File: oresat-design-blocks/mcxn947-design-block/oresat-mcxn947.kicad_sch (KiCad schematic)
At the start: 67 parts, among them J1 BKUP-BATT, J2 USB_C_Receptacle_USB2.0_14P, J3 CAN, J4 TERM, J5 10pin ARM SWD, J6 FTDI-UART-6PIN, SW1 RESET, SW2 ISP(BOOT), U1 MCXN947VKLT, U2 TCAN330, Y1 24 MHz, Y2 32.768 KHz

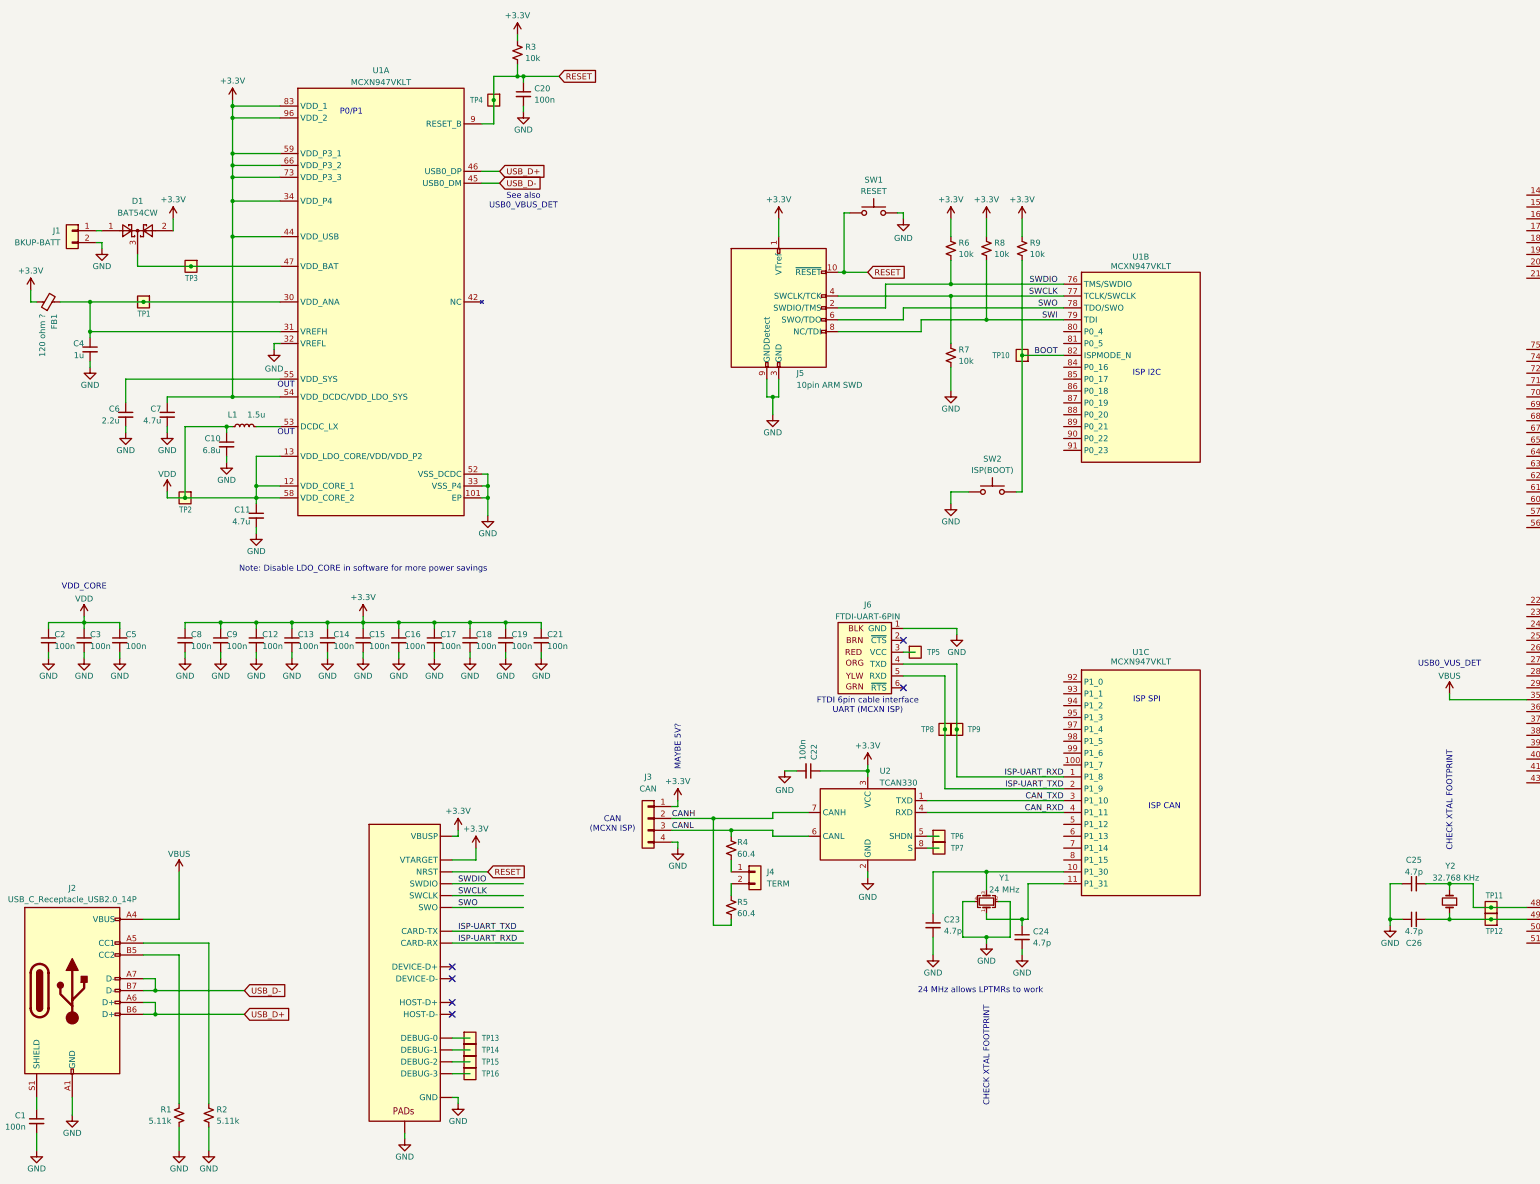
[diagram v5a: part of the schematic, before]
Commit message: Added 3.3V SPS but not hooked up yet. Everything else a rough draft, except for pin breakouts.
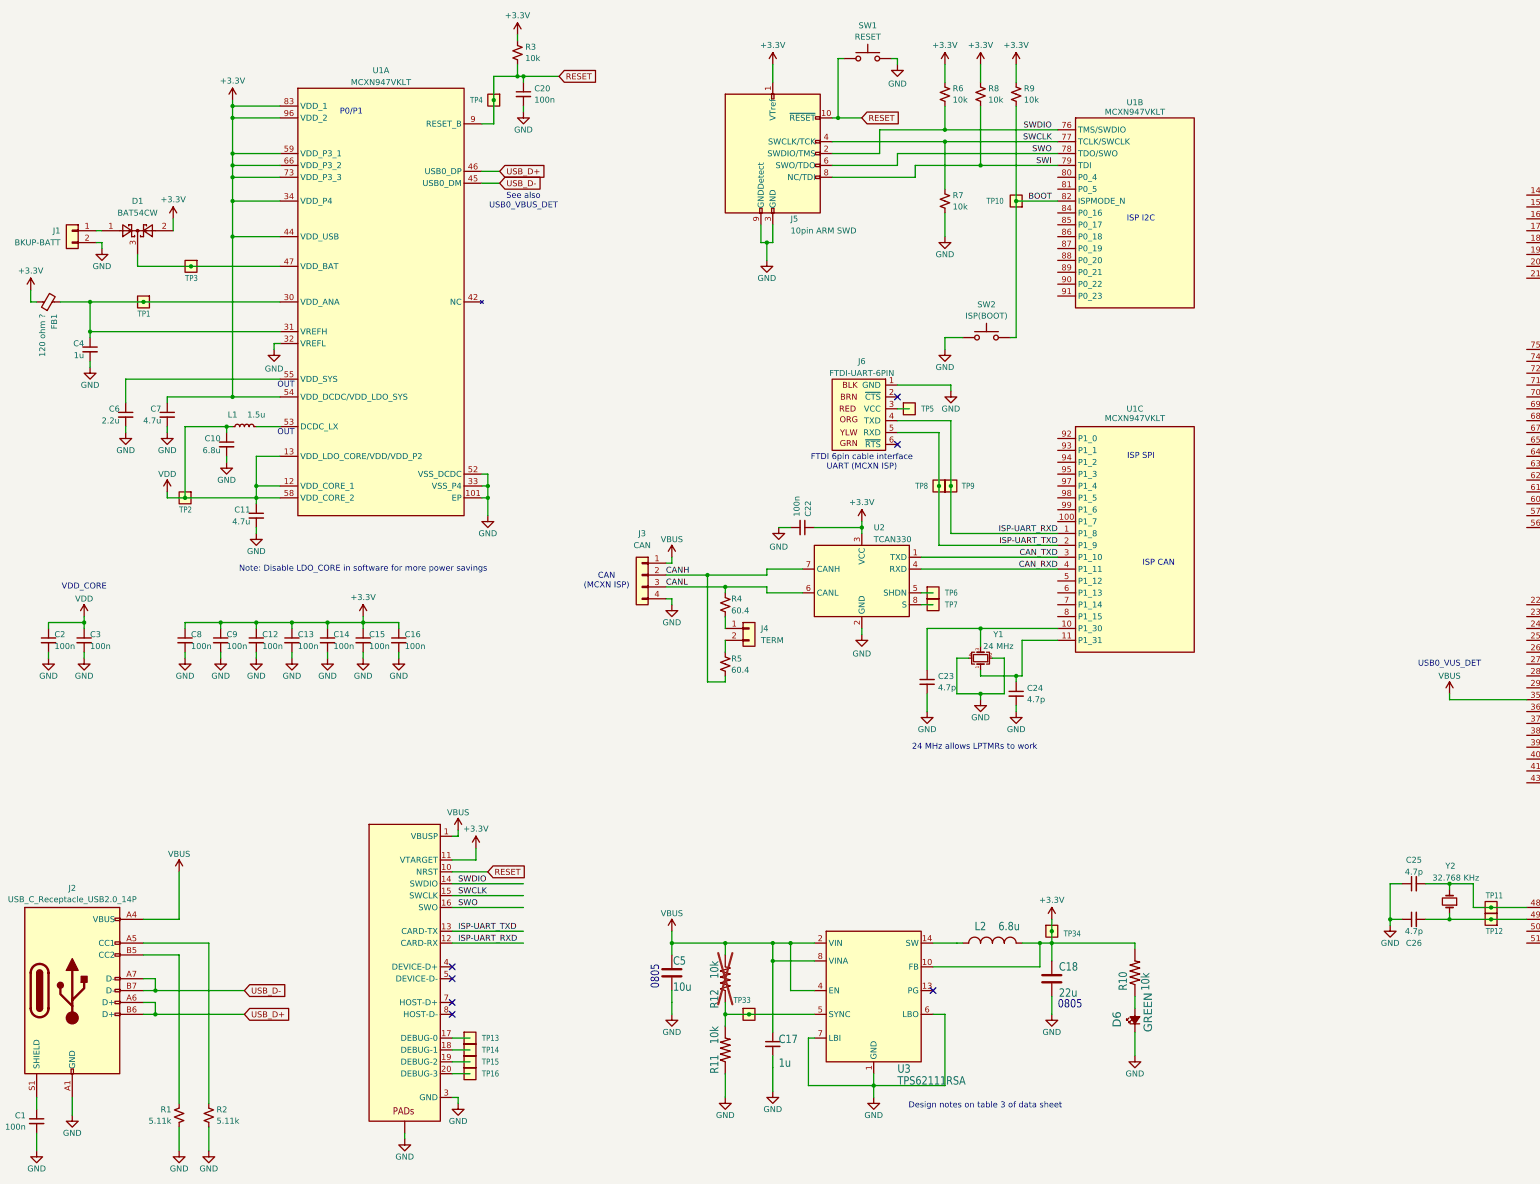
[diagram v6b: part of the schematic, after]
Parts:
- removed C18, C19, C21, C5: 100n, oresat-passives:0603-B-NOSILK, symbol Device:C_Small
- added C18: 22u, oresat-passives:0805-B-NOSILK, symbol Device:C
- added C5: 10u, oresat-passives:0805-B-NOSILK, symbol Device:C
- added D6: GREEN, LED_SMD:LED_0603_1608Metric, symbol Device:LED_Small_Filled
- added L2: 6.8u, oresat-passives:L_ECS-MPI4040, symbol oresat-passives:L_BIG
- added R10, R11, R12: 10k, oresat-passives:0603-C-NOSILK, symbol oresat-passives:R-US
- added TP33, TP34: Test-Point, oresat-misc:TestPoint-0.75mm-th, symbol oresat-misc:Test-Point-0.75mm-th
- added U3: TPS62111RSA, Package_DFN_QFN:Texas_RSA_VQFN-16-1EP_4x4mm_P0.65mm_EP2.7x2.7mm, symbol oresat-ics:TPS6211X
- C17: value 100n -> 1u; footprint oresat-passives:0603-B-NOSILK -> oresat-passives:0603-C-NOSILK; DIS (none) -> Digi-Key; DPN (none) -> 311-1444-1-ND; MFR (none) -> Yageo; MPN (none) -> CC0603KRX5R7BB105
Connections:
- net +3.3V: now also C18.1, L2.2, R10.2, TP34.1, U3.10 (FB); no longer C17.1, J3.1 (Pin_1), J7.1 (VBUSP), J7.2 (VBUSP)
- net GND: now also C18.2, C5.2, D6.1 (K), R11.1, U3.1 (GND), U3.11 (GND), U3.12 (GND), U3.16 (GND), U3.17 (GND), U3.6 (LBO), U3.7 (LBI), U3.9 (GND)
- net VBUS: now also C17.1, J3.1 (Pin_1), J7.1 (VBUSP), J7.2 (VBUSP), C5.1, R12.2, U3.2 (VIN), U3.3 (VIN), U3.4 (EN), U3.8 (VINA)
- new net: L2.1, U3.14 (SW), U3.15 (SW)
- new net: R11.2, R12.1, TP33.1, U3.5 (SYNC)
- new net: D6.2 (A), R10.1
- no-connect marks 6 -> 7
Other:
- note added: "0805"
- note added: "Design notes on table 3 of data sheet"
- note removed: "CHECK XTAL FOOTPRINT"
- note removed: "MAYBE 5V?"
- moved on the sheet: C22, C23, C24, J3, J4, J5, J6, R4, R5, R6, R7, R8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

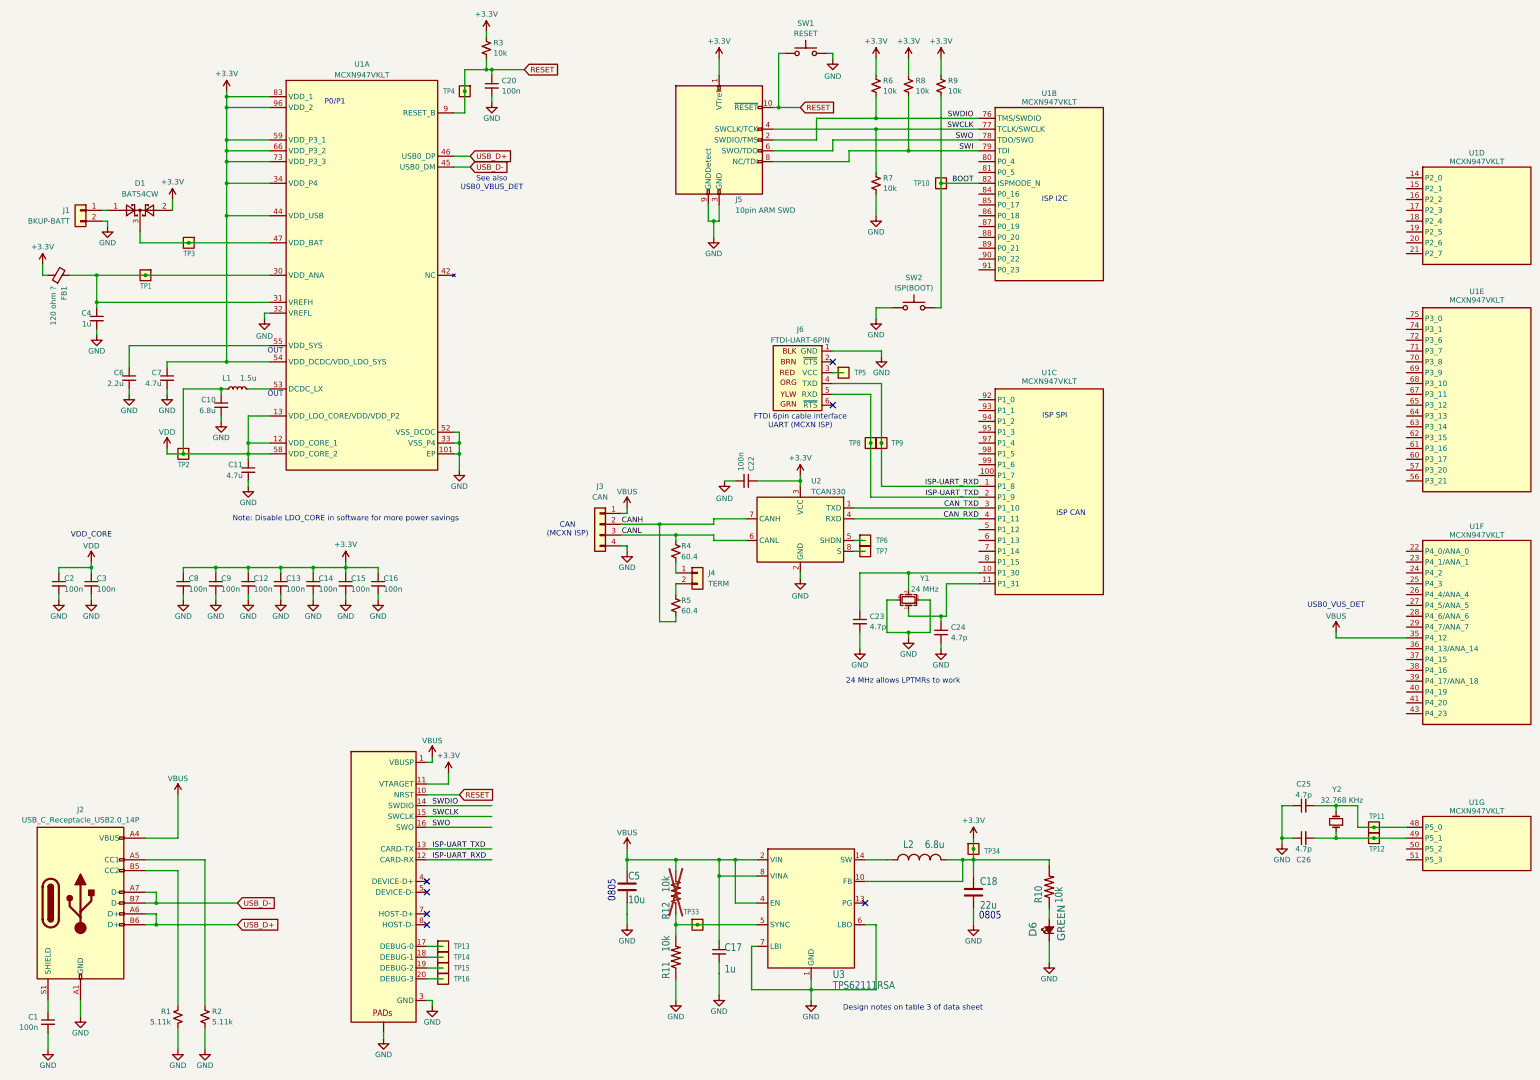
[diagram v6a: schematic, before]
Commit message: added hierarchal sheets, cleaned up schematic, added and routed breakout connectors
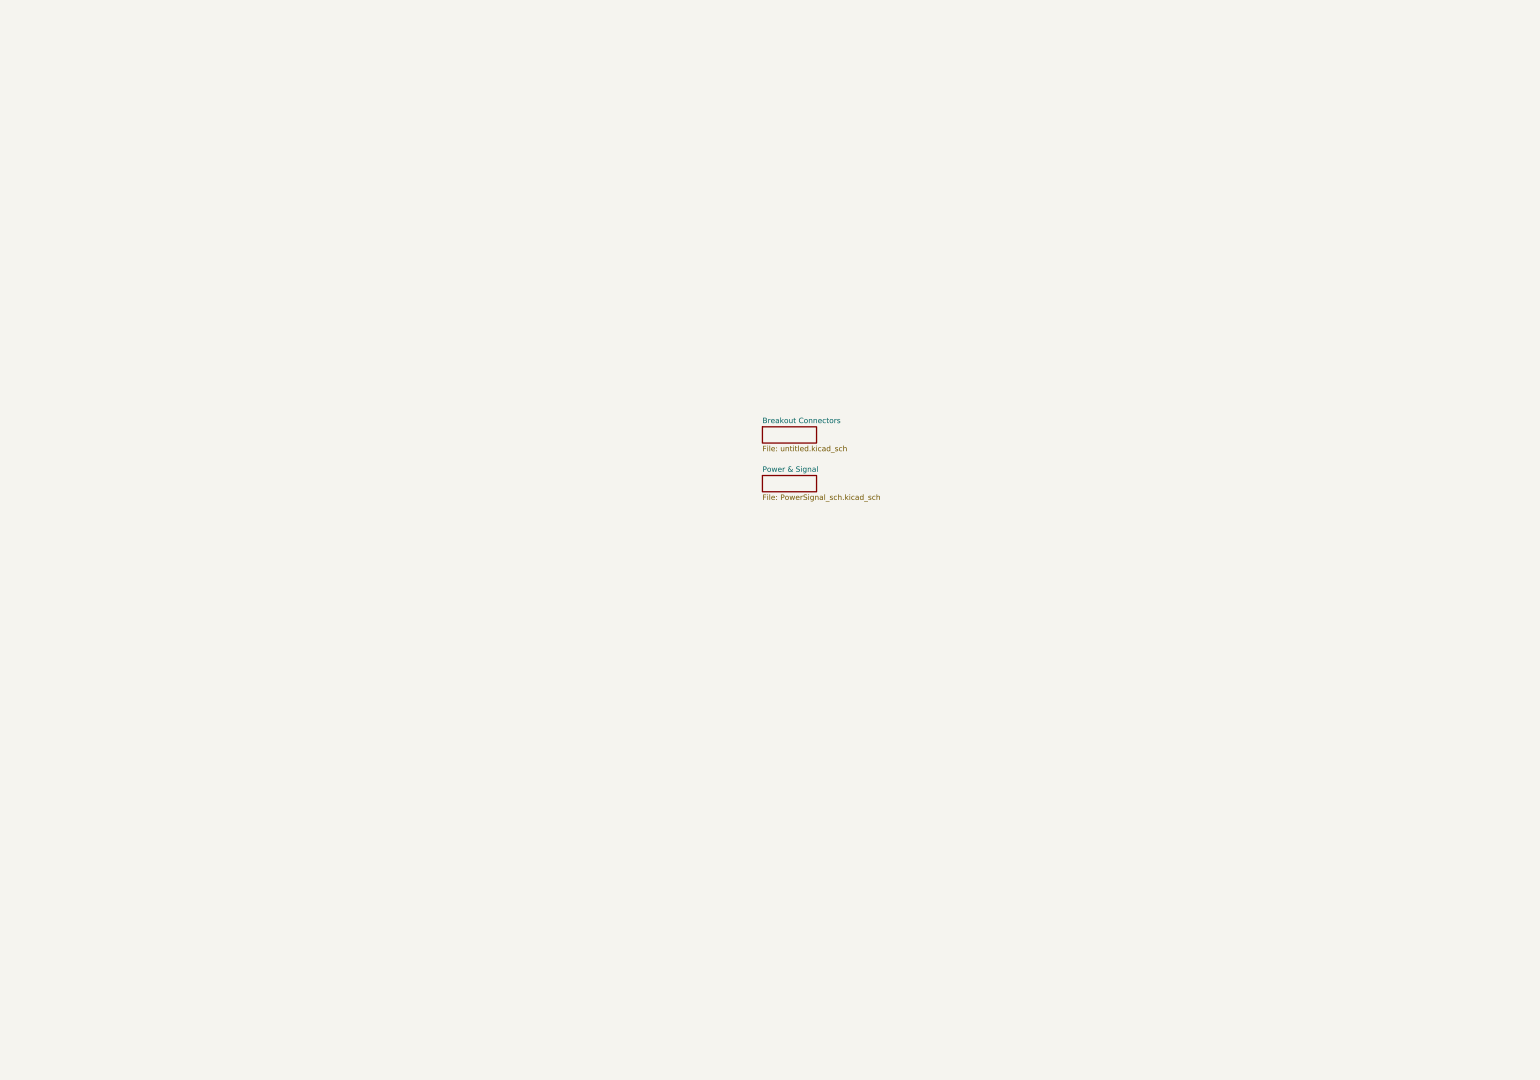
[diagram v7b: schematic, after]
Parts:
- removed C1, C12, C13, C14, C15, C16, C2, C20, C22, C3, C8, C9: 100n, oresat-passives:0603-B-NOSILK, symbol Device:C_Small
- removed C10: 6.8u, oresat-passives:0603-B-NOSILK, symbol Device:C_Small
- removed C11, C7: 4.7u, oresat-passives:0603-B-NOSILK, symbol Device:C_Small
- removed C17: 1u, oresat-passives:0603-C-NOSILK, symbol Device:C_Small
- removed C18: 22u, oresat-passives:0805-B-NOSILK, symbol Device:C
- removed C23, C24, C25, C26: 4.7p, oresat-passives:0603-B-NOSILK, symbol Device:C_Small
- removed C4: 1u, oresat-passives:0603-B-NOSILK, symbol Device:C_Small
- removed C5: 10u, oresat-passives:0805-B-NOSILK, symbol Device:C
- removed C6: 2.2u, oresat-passives:0603-B-NOSILK, symbol Device:C_Small
- removed D1: BAT54CW, oresat-passives:PAT0816(0603), symbol Diode:BAT54CW
- removed D6: GREEN, LED_SMD:LED_0603_1608Metric, symbol Device:LED_Small_Filled
- removed FB1: 120 ohm ?, oresat-passives:0805-B-NOSILK, symbol Device:FerriteBead_Small
- removed J1: BKUP-BATT, Connector_PinHeader_2.54mm:PinHeader_1x02_P2.54mm_Vertical, symbol Connector_Generic:Conn_01x02
- removed J2: USB_C_Receptacle_USB2.0_14P, Connector_USB:USB_C_Receptacle_Palconn_UTC16-G, symbol Connector:USB_C_Receptacle_USB2.0_14P
- removed J3: CAN, Connector_PinHeader_2.54mm:PinHeader_1x04_P2.54mm_Vertical, symbol Connector_Generic:Conn_01x04
- removed J4: TERM, Connector_PinHeader_2.54mm:PinHeader_1x02_P2.54mm_Vertical, symbol Connector_Generic:Conn_01x02
- removed J5: 10pin ARM SWD, Connector_PinHeader_1.27mm:PinHeader_2x05_P1.27mm_Vertical, symbol Connector:Conn_ARM_JTAG_SWD_10
- removed J6: FTDI-UART-6PIN, Connector_PinHeader_2.54mm:PinHeader_1x06_P2.54mm_Vertical, symbol oresat-connectors:FTDI-UART-6PIN
- removed J7: ~, oresat-connectors:J-TE-2-1734592-0, symbol oresat-connectors:ORESAT-DEBUG-CONNECTOR-ALL
- removed L1: 1.5u, Inductor_SMD:L_0805_2012Metric, symbol Device:L_Small
- removed L2: 6.8u, oresat-passives:L_ECS-MPI4040, symbol oresat-passives:L_BIG
- removed R1, R2: 5.11k, oresat-passives:0603-B-NOSILK, symbol Device:R_Small_US
- removed R10, R11, R12: 10k, oresat-passives:0603-C-NOSILK, symbol oresat-passives:R-US
- removed R3, R6, R7, R8, R9: 10k, oresat-passives:0603-B-NOSILK, symbol Device:R_Small_US
- removed R4, R5: 60.4, oresat-passives:0603-B-NOSILK, symbol Device:R_Small_US
- removed SW1: RESET, Button_Switch_THT:SW_PUSH_6mm, symbol Switch:SW_Push
- removed SW2: ISP(BOOT), Button_Switch_THT:SW_PUSH_6mm, symbol Switch:SW_Push
- removed TP1, TP10, TP11, TP12, TP13, TP14, TP15, TP16, TP2, TP3, TP33, TP34, TP4, TP5, TP6, TP7, TP8, TP9: Test-Point, oresat-misc:TestPoint-0.75mm-th, symbol oresat-misc:Test-Point-0.75mm-th
- removed U1: MCXN947VKLT, oresat-ics:MCXN947KVLT-QFP50P1600X1600X160-101N, symbol oresat-ics:MCXN947VKLT
- removed U2: TCAN330, Package_TO_SOT_SMD:SOT-23-8, symbol Interface_CAN_LIN:TCAN330
- removed U3: TPS62111RSA, Package_DFN_QFN:Texas_RSA_VQFN-16-1EP_4x4mm_P0.65mm_EP2.7x2.7mm, symbol oresat-ics:TPS6211X
- removed Y1: 24 MHz, Crystal:Crystal_SMD_2016-4Pin_2.0x1.6mm, symbol Device:Crystal_GND24_Small
- removed Y2: 32.768 KHz, Crystal:Crystal_SMD_3215-2Pin_3.2x1.5mm, symbol Device:Crystal_Small
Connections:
- no-connect marks 7 -> 0
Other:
- added sheet Breakout Connectors (untitled.kicad_sch)
- added sheet Power & Signal (PowerSignal_sch.kicad_sch)
- note removed: "0805"
- note removed: "24 MHz allows LPTMRs to work"
- note removed: "CAN (MCXN ISP)"
- note removed: "Design notes on table 3 of data sheet"
- note removed: "FTDI 6pin cable interface UART (MCXN ISP)"
- note removed: "ISP CAN"
- note removed: "ISP I2C"
- note removed: "ISP SPI"
- note removed: "Note: Disable LDO_CORE in software for more power savings"
- note removed: "OUT"
- note removed: "P0/P1"
- note removed: "See also USB0_VBUS_DET"
- note removed: "USB0_VUS_DET"
- note removed: "VDD_CORE"
